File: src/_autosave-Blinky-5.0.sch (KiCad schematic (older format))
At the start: 8 parts, among them U1 7555

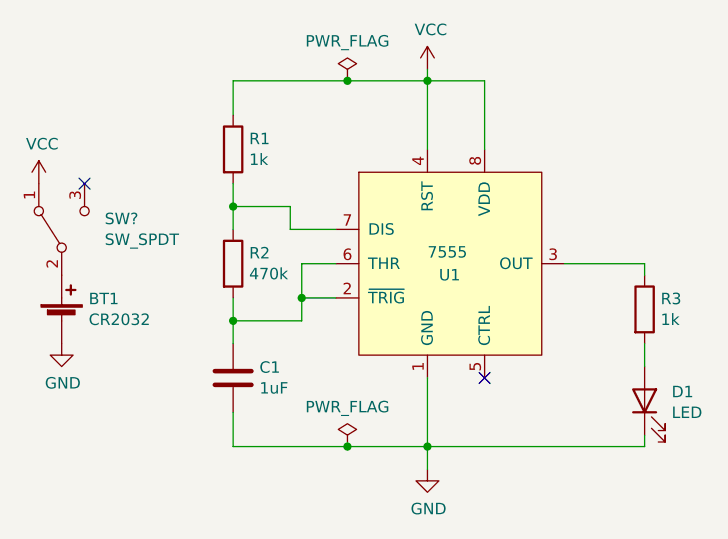
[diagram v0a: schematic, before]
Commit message: Make some custom footprints and define board layout
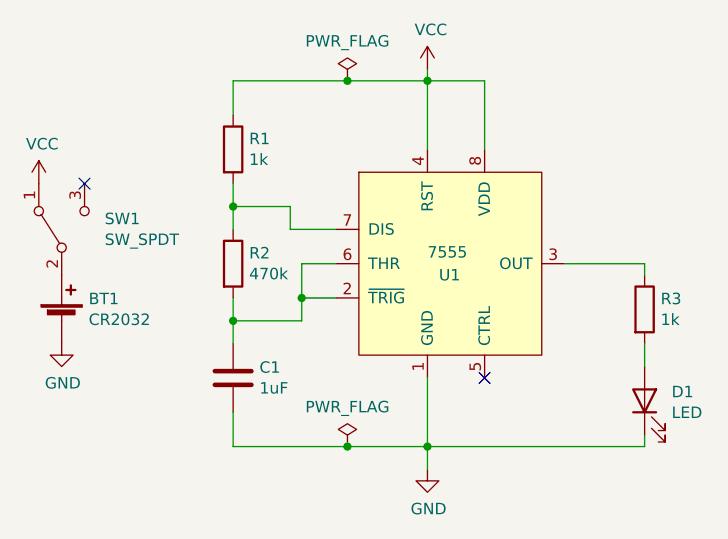
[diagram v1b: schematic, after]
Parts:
- SW1: renamed from SW?; footprint (none) -> src:JS102011SCQN
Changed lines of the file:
@@
 $EndComp
 $Comp
-L power:VCC #PWR0101
+L power:VCC #PWR0103
 U 1 1 609313FA
 P 5400 2950
-F 0 "#PWR0101" H 5400 2800 50  0001 C CNN
+F 0 "#PWR0103" H 5400 2800 50  0001 C CNN
 F 1 "VCC" H 5415 3123 50  0000 C CNN
 F 2 "" H 5400 2950 50  0001 C CNN
@@
 	5400 3000 5400 2950
 $Comp
-L power:GND #PWR0102
+L power:GND #PWR0104
 U 1 1 6093A498
 P 5400 4700
-F 0 "#PWR0102" H 5400 4450 50  0001 C CNN
+F 0 "#PWR0104" H 5400 4450 50  0001 C CNN
 F 1 "GND" H 5405 4527 50  0000 C CNN
 F 2 "" H 5400 4700 50  0001 C CNN
@@
 	5050 4600 5400 4600
 $Comp
-L Switch:SW_SPDT SW?
+L Switch:SW_SPDT SW1
 U 1 1 6096FD5C
 P 3800 3650
-F 0 "SW?" V 3846 3462 50  0000 R CNN
+F 0 "SW1" V 3846 3462 50  0000 R CNN
 F 1 "SW_SPDT" V 3755 3462 50  0000 R CNN
-F 2 "" H 3800 3650 50  0001 C CNN
+F 2 "src:JS102011SCQN" H 3800 3650 50  0001 C CNN
 F 3 "~" H 3800 3650 50  0001 C CNN
 	1    3800 3650
